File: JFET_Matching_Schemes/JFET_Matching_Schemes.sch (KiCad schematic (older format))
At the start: 0 parts

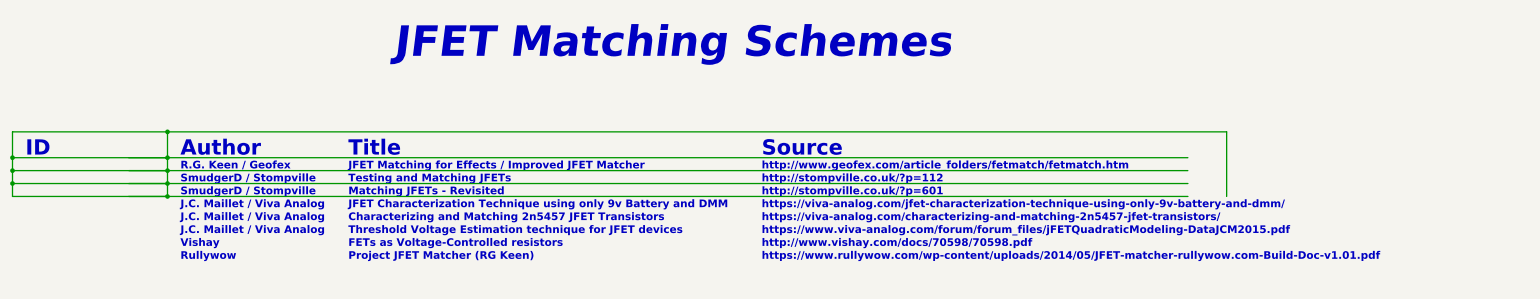
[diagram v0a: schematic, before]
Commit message: updated jfet matching scheme, eng. thumb. symbol rescue
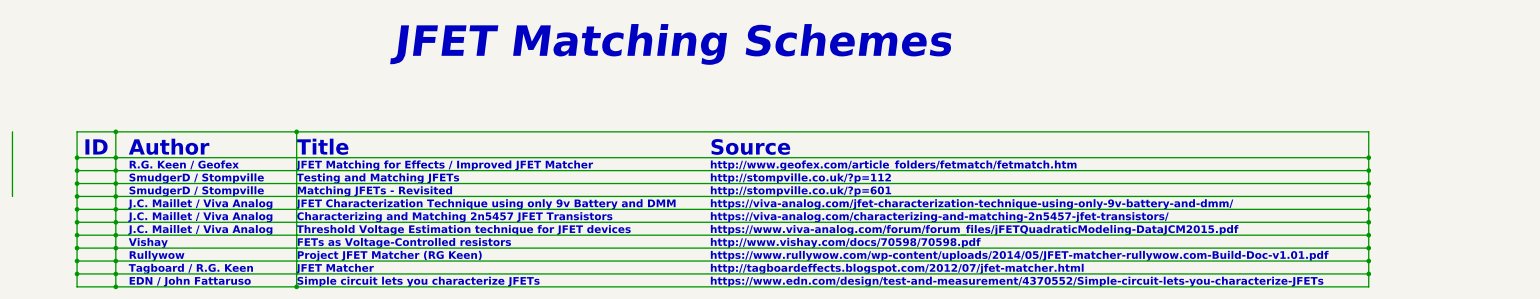
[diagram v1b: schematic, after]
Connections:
- wire segments 23 -> 61
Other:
- note added: "EDN / John Fattaruso"
- note added: "JFET Matcher"
- note added: "Simple circuit lets you characterize JFETs"
- note added: "Tagboard / R.G. Keen"
- note added: "http://tagboardeffects.blogspot.com/2012/07/jfet-matcher.html"
- note added: "https://www.edn.com/design/test-and-measurement/4370552/Simple-circuit-lets-you-characterize-JFETs"
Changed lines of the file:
@@
 EESchema Schematic File Version 4
+LIBS:JFET_Matching_Schemes-cache
 EELAYER 26 0
 EELAYER END
@@
 Text Notes 3350 1450 0    236  Italic 47
 JFET Matching Schemes
-Text Notes 6200 2300 0    59   ~ 12
+Text Notes 5800 2300 0    59   ~ 12
 http://www.geofex.com/article_folders/fetmatch/fetmatch.htm
-Text Notes 500  2200 0    118  ~ 24
+Text Notes 950  2200 0    118  ~ 24
 ID
-Text Notes 1700 2200 0    118  ~ 24
+Text Notes 1300 2200 0    118  ~ 24
 Author
-Text Notes 6200 2200 0    118  ~ 24
+Text Notes 5800 2200 0    118  ~ 24
 Source
-Text Notes 1700 2300 0    59   ~ 12
+Text Notes 1300 2300 0    59   ~ 12
 R.G. Keen / Geofex
 Wire Wire Line
-	400  2000 400  2200
-Wire Wire Line
-	400  2000 1600 2000
-Wire Wire Line
-	1600 2200 1600 2000
-Connection ~ 1600 2200
-Connection ~ 1600 2000
-Wire Wire Line
-	1600 2000 9800 2000
-Text Notes 3000 2200 0    118  ~ 24
+	1200 2200 1200 2000
+Connection ~ 1200 2200
+Text Notes 2600 2200 0    118  ~ 24
 Title
-Text Notes 3000 2300 0    59   ~ 12
+Text Notes 2600 2300 0    59   ~ 12
 JFET Matching for Effects / Improved JFET Matcher
-Text Notes 6200 2400 0    59   ~ 12
+Text Notes 5800 2400 0    59   ~ 12
 http://stompville.co.uk/?p=112
 Wire Wire Line
-	400  2200 400  2300
-Connection ~ 400  2200
-Wire Wire Line
-	9500 2400 1600 2400
-Wire Wire Line
-	400  2400 400  2300
-Connection ~ 400  2300
-Wire Wire Line
-	1600 2400 1600 2300
-Connection ~ 1600 2400
-Connection ~ 1600 2300
-Wire Wire Line
-	1600 2300 1600 2200
-Text Notes 3000 2400 0    59   ~ 12
+	1200 2400 1200 2300
+Connection ~ 1200 2400
+Connection ~ 1200 2300
+Wire Wire Line
+	1200 2300 1200 2200
+Text Notes 2600 2400 0    59   ~ 12
 Testing and Matching JFETs
-Text Notes 1700 2400 0    59   ~ 12
+Text Notes 1300 2400 0    59   ~ 12
 SmudgerD / Stompville
-Text Notes 3000 2500 0    59   ~ 12
+Text Notes 2600 2500 0    59   ~ 12
 Matching JFETs - Revisited
-Text Notes 1700 2500 0    59   ~ 12
+Text Notes 1300 2500 0    59   ~ 12
 SmudgerD / Stompville
-Text Notes 6200 2500 0    59   ~ 12
+Text Notes 5800 2500 0    59   ~ 12
 http://stompville.co.uk/?p=601
 Wire Wire Line
-	9500 2500 1600 2500
-Wire Wire Line
-	400  2500 400  2400
-Connection ~ 400  2400
-Wire Wire Line
-	1600 2400 1600 2500
-Connection ~ 1600 2500
-Text Notes 6200 2600 0    59   ~ 12
+	1200 2400 1200 2500
+Text Notes 5800 2600 0    59   ~ 12
 https://viva-analog.com/jfet-characterization-technique-using-only-9v-battery-and-dmm/
-Text Notes 3000 2600 0    59   ~ 12
+Text Notes 2600 2600 0    59   ~ 12
 JFET Characterization Technique using only 9v Battery and DMM
-Text Notes 1700 2600 0    59   ~ 12
+Text Notes 1300 2600 0    59   ~ 12
 J.C. Maillet / Viva Analog
-Text Notes 1700 2700 0    59   ~ 12
+Text Notes 1300 2700 0    59   ~ 12
 J.C. Maillet / Viva Analog
-Text Notes 6200 2700 0    59   ~ 12
+Text Notes 5800 2700 0    59   ~ 12
 https://viva-analog.com/characterizing-and-matching-2n5457-jfet-transistors/
-Text Notes 3000 2700 0    59   ~ 12
+Text Notes 2600 2700 0    59   ~ 12
 Characterizing and Matching 2n5457 JFET Transistors
-Text Notes 3000 2900 0    59   ~ 12
+Text Notes 2600 2900 0    59   ~ 12
 FETs as Voltage-Controlled resistors
-Text Notes 1700 2900 0    59   ~ 12
+Text Notes 1300 2900 0    59   ~ 12
 Vishay
-Text Notes 6200 2900 0    59   ~ 12
+Text Notes 5800 2900 0    59   ~ 12
 http://www.vishay.com/docs/70598/70598.pdf
-Text Notes 3000 2800 0    59   ~ 12
+Text Notes 2600 2800 0    59   ~ 12
 Threshold Voltage Estimation technique for JFET devices
-Text Notes 6200 2800 0    59   ~ 12
+Text Notes 5800 2800 0    59   ~ 12
 https://www.viva-analog.com/forum/forum_files/jFETQuadraticModeling-DataJCM2015.pdf
-Text Notes 1700 2800 0    59   ~ 12
+Text Notes 1300 2800 0    59   ~ 12
 J.C. Maillet / Viva Analog
-Text Notes 1700 3000 0    59   ~ 12
+Text Notes 1300 3000 0    59   ~ 12
 Rullywow
-Text Notes 3000 3000 0    59   ~ 12
+Text Notes 2600 3000 0    59   ~ 12
 Project JFET Matcher (RG Keen)
-Text Notes 6200 3000 0    59   ~ 12
+Text Notes 5800 3000 0    59   ~ 12
 https://www.rullywow.com/wp-content/uploads/2014/05/JFET-matcher-rullywow.com-Build-Doc-v1.01.pdf
-Wire Wire Line
-	1600 2200 9500 2200
-Wire Wire Line
-	1600 2300 9500 2300
-Wire Wire Line
-	9800 2000 9800 2500
-Wire Wire Line
-	1300 2200 1600 2200
-Wire Wire Line
-	1300 2300 1600 2300
-Wire Wire Line
-	1300 2400 1600 2400
-Wire Wire Line
-	1300 2500 1600 2500
-Wire Wire Line
-	400  2200 1600 2200
-Wire Wire Line
-	400  2300 1600 2300
-Wire Wire Line
-	400  2400 1600 2400
-Wire Wire Line
-	400  2500 1600 2500
+Text Notes 5800 3100 0    59   ~ 12
+http://tagboardeffects.blogspot.com/2012/07/jfet-matcher.html
+Text Notes 2600 3100 0    59   ~ 12
+JFET Matcher
+Text Notes 1300 3100 0    59   ~ 12
+Tagboard / R.G. Keen
+Text Notes 5800 3200 0    59   ~ 12
+https://www.edn.com/design/test-and-measurement/4370552/Simple-circuit-lets-you-characterize-JFETs
+Text Notes 2600 3200 0    59   ~ 12
+Simple circuit lets you characterize JFETs
+Text Notes 1300 3200 0    59   ~ 12
+EDN / John Fattaruso
+Wire Wire Line
+	400  2000 400  2500
+Wire Wire Line
+	1200 2200 900  2200
+Wire Wire Line
+	900  2200 900  2000
+Wire Wire Line
+	900  2000 1200 2000
+Connection ~ 1200 2000
+Wire Wire Line
+	1200 2500 1200 2600
+Wire Wire Line
+	1200 2600 10900 2600
+Wire Wire Line
+	10900 2600 10900 2500
+Connection ~ 1200 2500
+Wire Wire Line
+	1200 2500 10900 2500
+Wire Wire Line
+	10900 2400 10900 2500
+Wire Wire Line
+	1200 2400 10900 2400
+Connection ~ 10900 2500
+Wire Wire Line
+	10900 2400 10900 2300
+Wire Wire Line
+	1200 2300 10900 2300
+Connection ~ 10900 2400
+Wire Wire Line
+	10900 2200 10900 2300
+Wire Wire Line
+	1200 2200 10900 2200
+Connection ~ 10900 2300
+Wire Wire Line
+	10900 2200 10900 2000
+Wire Wire Line
+	1200 2000 2600 2000
+Connection ~ 10900 2200
+Wire Wire Line
+	2600 2000 2600 3200
+Wire Wire Line
+	1200 3200 1200 3100
+Connection ~ 2600 2000
+Wire Wire Line
+	2600 2000 10900 2000
+Connection ~ 1200 2600
+Wire Wire Line
+	1200 2700 10900 2700
+Wire Wire Line
+	10900 2700 10900 2600
+Connection ~ 1200 2700
+Wire Wire Line
+	1200 2700 1200 2600
+Connection ~ 10900 2600
+Wire Wire Line
+	10900 2700 10900 2800
+Wire Wire Line
+	10900 2800 1200 2800
+Connection ~ 10900 2700
+Connection ~ 1200 2800
+Wire Wire Line
+	1200 2800 1200 2700
+Wire Wire Line
+	1200 2900 10900 2900
+Wire Wire Line
+	10900 2900 10900 2800
+Connection ~ 1200 2900
+Wire Wire Line
+	1200 2900 1200 2800
+Connection ~ 10900 2800
+Wire Wire Line
+	10900 2900 10900 3000
+Wire Wire Line
+	10900 3000 1200 3000
+Connection ~ 10900 2900
+Connection ~ 1200 3000
+Wire Wire Line
+	1200 3000 1200 2900
+Wire Wire Line
+	1200 3100 10900 3100
+Wire Wire Line
+	10900 3100 10900 3000
+Connection ~ 1200 3100
+Wire Wire Line
+	1200 3100 1200 3000
+Connection ~ 10900 3000
+Wire Wire Line
+	1200 3200 2600 3200
+Wire Wire Line
+	10900 3200 10900 3100
+Connection ~ 2600 3200
+Wire Wire Line
+	2600 3200 10900 3200
+Connection ~ 10900 3100
+Wire Wire Line
+	1200 3200 900  3200
+Wire Wire Line
+	900  3200 900  3100
+Connection ~ 1200 3200
+Connection ~ 900  2200
+Wire Wire Line
+	900  2300 1200 2300
+Connection ~ 900  2300
+Wire Wire Line
+	900  2300 900  2200
+Wire Wire Line
+	1200 2400 900  2400
+Connection ~ 900  2400
+Wire Wire Line
+	900  2400 900  2300
+Wire Wire Line
+	900  2500 1200 2500
+Connection ~ 900  2500
+Wire Wire Line
+	900  2500 900  2400
+Wire Wire Line
+	1200 2600 900  2600
+Connection ~ 900  2600
+Wire Wire Line
+	900  2600 900  2500
+Wire Wire Line
+	900  2700 1200 2700
+Connection ~ 900  2700
+Wire Wire Line
+	900  2700 900  2600
+Wire Wire Line
+	1200 2800 900  2800
+Connection ~ 900  2800
+Wire Wire Line
+	900  2800 900  2700
+Wire Wire Line
+	900  2900 1200 2900
+Connection ~ 900  2900
+Wire Wire Line
+	900  2900 900  2800
+Wire Wire Line
+	1200 3000 900  3000
+Connection ~ 900  3000
+Wire Wire Line
+	900  3000 900  2900
+Wire Wire Line
+	900  3100 1200 3100
+Connection ~ 900  3100
+Wire Wire Line
+	900  3100 900  3000
 $EndSCHEMATC
